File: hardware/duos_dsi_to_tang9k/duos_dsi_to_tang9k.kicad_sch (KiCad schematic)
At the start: 6 parts, among them J1 Duo_S_DSI_IN, J2 Tang_Nano_9K

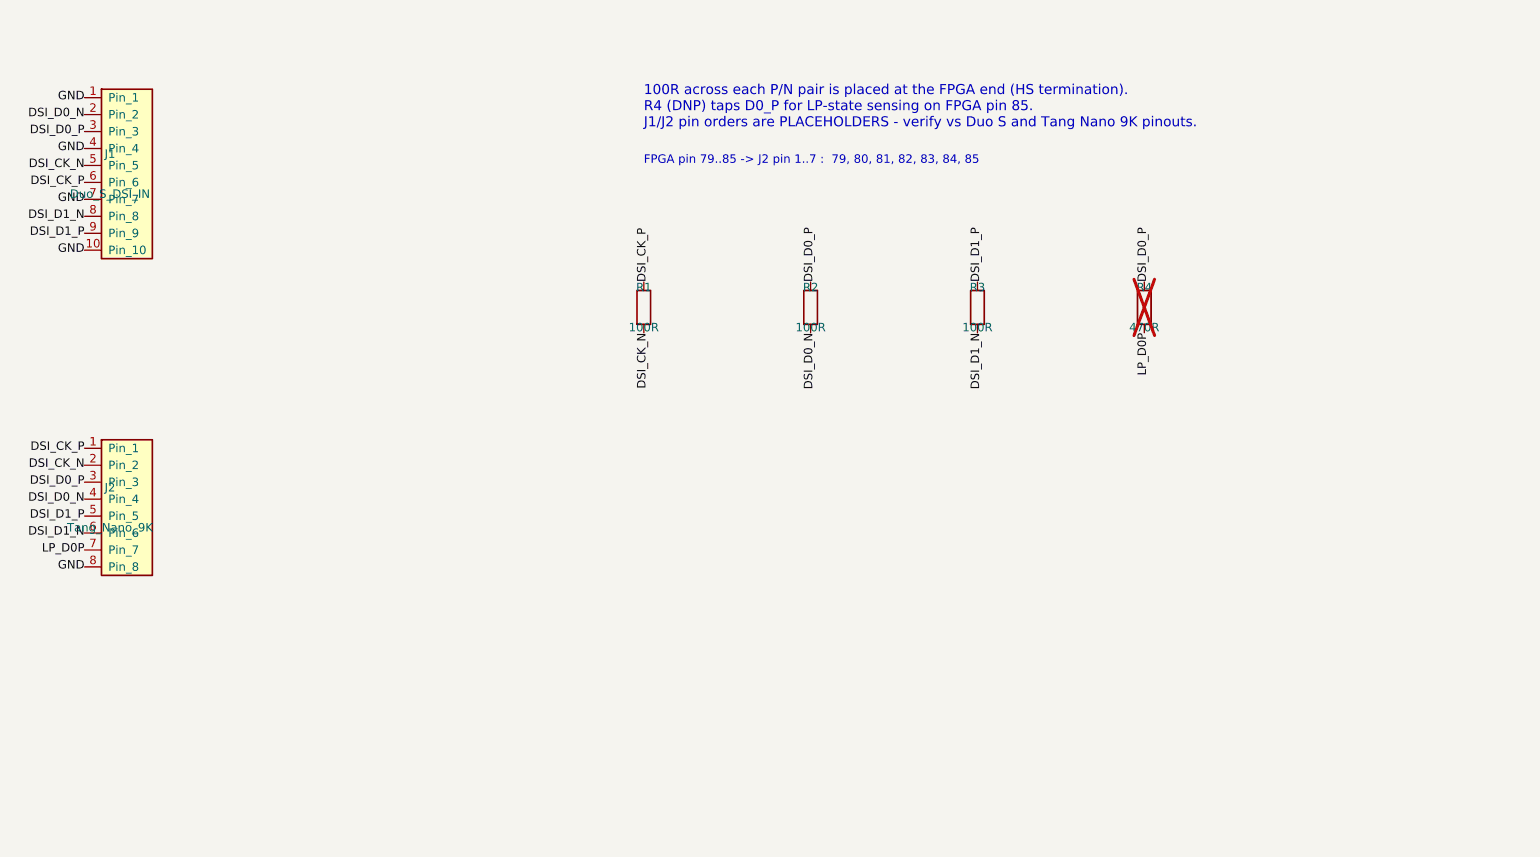
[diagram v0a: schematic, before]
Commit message: Use real Duo S CON26A MIPI_TX pinout in DSI adapter project
Co-Authored-By: Claude Sonnet 5.5 <noreply@anthropic.com>
Claude-Session: https://claude.ai/code/session_01Kmp7iiQhgLgwfNawdP6KaV
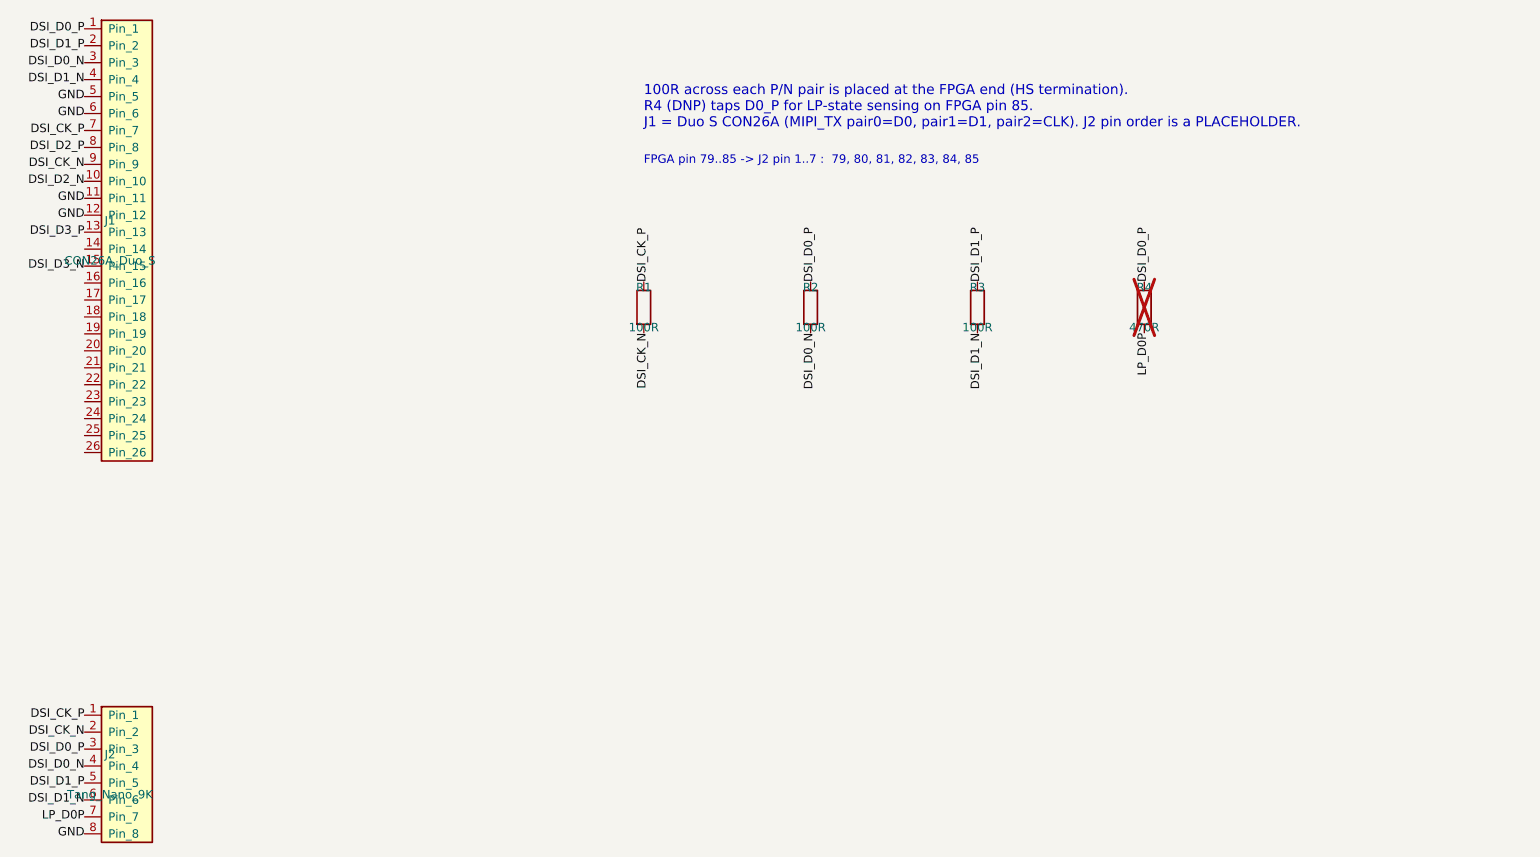
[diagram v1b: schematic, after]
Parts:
- removed J1: Duo_S_DSI_IN, Connector_PinHeader_2.54mm:PinHeader_1x10_P2.54mm_Vertical, symbol Connector_Generic:Conn_01x10
- added J1: CON26A_Duo_S, Connector_PinHeader_2.54mm:PinHeader_2x13_P2.54mm_Vertical, symbol Connector_Generic:Conn_01x26
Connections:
- net DSI_CK_N: now also J1.9 (Pin_9)
- net DSI_CK_P: now also J1.7 (Pin_7)
- net DSI_D0_N: now also J1.3 (Pin_3)
- net DSI_D0_P: now also J1.1 (Pin_1)
- net DSI_D1_N: now also J1.4 (Pin_4)
- net DSI_D1_P: now also J1.2 (Pin_2)
- net GND: now also J1.11 (Pin_11), J1.12 (Pin_12), J1.5 (Pin_5), J1.6 (Pin_6)
- new net DSI_D2_N: J1.10 (Pin_10)
- new net DSI_D2_P: J1.8 (Pin_8)
- new net DSI_D3_N: J1.15 (Pin_15)
- new net DSI_D3_P: J1.13 (Pin_13)
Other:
- note added: "100R across each P/N pair is placed at the FPGA end (HS termination). R4 (DNP) taps D0_P for LP-state sensing on FPGA pin 85. J1 = Duo S CON26A (MIPI_TX pair0=D0, pair1=D1, pair2=CLK). J2 pin order is a PLACEHOLDER."
- note removed: "100R across each P/N pair is placed at the FPGA end (HS termination). R4 (DNP) taps D0_P for LP-state sensing on FPGA pin 85. J1/J2 pin orders are PLACEHOLDERS - verify vs Duo S and Tang Nano 9K pinouts."
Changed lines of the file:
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@@
 (kicad_sch (version 20230121) (generator "gen_project.py") (paper "A4")
-(symbol (lib_id "Connector_Generic:Conn_01x10") (at 60 80 0) (unit 1) (in_bom yes) (on_board yes) (dnp no)
-(property "Reference" "J1" (at 60 77 0) (effects (font (size 1.27 1.27))))
-(property "Value" "Duo_S_DSI_IN" (at 60 83 0) (effects (font (size 1.27 1.27))))
-(property "Footprint" "Connector_PinHeader_2.54mm:PinHeader_1x10_P2.54mm_Vertical" (at 60 80 0) (effects (font (size 1.27 1.27)) hide))
-(pin "1")(pin "2")(pin "3")(pin "4")(pin "5")(pin "6")(pin "7")(pin "8")(pin "9")(pin "10")
-(instances (project "duos_dsi_to_tang9k" (path "/370e3fb2-c56f-42e8-af79-f2a3169dccd3" (reference "J1") (unit 1)))))
-(label "GND" (at 56.19 68.57 180) (effects (font (size 1.27 1.27)) (justify right)))
-(label "DSI_D0_N" (at 56.19 71.11 180) (effects (font (size 1.27 1.27)) (justify right)))
-(label "DSI_D0_P" (at 56.19 73.65 180) (effects (font (size 1.27 1.27)) (justify right)))
-(label "GND" (at 56.19 76.19 180) (effects (font (size 1.27 1.27)) (justify right)))
-(label "DSI_CK_N" (at 56.19 78.73 180) (effects (font (size 1.27 1.27)) (justify right)))
-(label "DSI_CK_P" (at 56.19 81.27 180) (effects (font (size 1.27 1.27)) (justify right)))
-(label "GND" (at 56.19 83.81 180) (effects (font (size 1.27 1.27)) (justify right)))
-(label "DSI_D1_N" (at 56.19 86.35 180) (effects (font (size 1.27 1.27)) (justify right)))
-(label "DSI_D1_P" (at 56.19 88.89 180) (effects (font (size 1.27 1.27)) (justify right)))
-(label "GND" (at 56.19 91.43 180) (effects (font (size 1.27 1.27)) (justify right)))
-(symbol (lib_id "Connector_Generic:Conn_01x08") (at 60 130 0) (unit 1) (in_bom yes) (on_board yes) (dnp no)
-(property "Reference" "J2" (at 60 127 0) (effects (font (size 1.27 1.27))))
-(property "Value" "Tang_Nano_9K" (at 60 133 0) (effects (font (size 1.27 1.27))))
-(property "Footprint" "Connector_PinHeader_2.54mm:PinHeader_1x08_P2.54mm_Vertical" (at 60 130 0) (effects (font (size 1.27 1.27)) hide))
+(symbol (lib_id "Connector_Generic:Conn_01x26") (at 60 90 0) (unit 1) (in_bom yes) (on_board yes) (dnp no)
+(property "Reference" "J1" (at 60 87 0) (effects (font (size 1.27 1.27))))
+(property "Value" "CON26A_Duo_S" (at 60 93 0) (effects (font (size 1.27 1.27))))
+(property "Footprint" "Connector_PinHeader_2.54mm:PinHeader_2x13_P2.54mm_Vertical" (at 60 90 0) (effects (font (size 1.27 1.27)) hide))
+(pin "1")(pin "2")(pin "3")(pin "4")(pin "5")(pin "6")(pin "7")(pin "8")(pin "9")(pin "10")(pin "11")(pin "12")(pin "13")(pin "14")(pin "15")(pin "16")(pin "17")(pin "18")(pin "19")(pin "20")(pin "21")(pin "22")(pin "23")(pin "24")(pin "25")(pin "26")
+(instances (project "duos_dsi_to_tang9k" (path "/7ba3984c-b53a-427d-af08-25dba6ae9ceb" (reference "J1") (unit 1)))))
+(label "DSI_D0_P" (at 56.19 58.25 180) (effects (font (size 1.27 1.27)) (justify right)))
+(label "DSI_D1_P" (at 56.19 60.79 180) (effects (font (size 1.27 1.27)) (justify right)))
+(label "DSI_D0_N" (at 56.19 63.33 180) (effects (font (size 1.27 1.27)) (justify right)))
+(label "DSI_D1_N" (at 56.19 65.87 180) (effects (font (size 1.27 1.27)) (justify right)))
+(label "GND" (at 56.19 68.41 180) (effects (font (size 1.27 1.27)) (justify right)))
+(label "GND" (at 56.19 70.95 180) (effects (font (size 1.27 1.27)) (justify right)))
+(label "DSI_CK_P" (at 56.19 73.49 180) (effects (font (size 1.27 1.27)) (justify right)))
+(label "DSI_D2_P" (at 56.19 76.03 180) (effects (font (size 1.27 1.27)) (justify right)))
+(label "DSI_CK_N" (at 56.19 78.57 180) (effects (font (size 1.27 1.27)) (justify right)))
+(label "DSI_D2_N" (at 56.19 81.11 180) (effects (font (size 1.27 1.27)) (justify right)))
+(label "GND" (at 56.19 83.65 180) (effects (font (size 1.27 1.27)) (justify right)))
+(label "GND" (at 56.19 86.19 180) (effects (font (size 1.27 1.27)) (justify right)))
+(label "DSI_D3_P" (at 56.19 88.73 180) (effects (font (size 1.27 1.27)) (justify right)))
+(label "DSI_D3_N" (at 56.19 93.81 180) (effects (font (size 1.27 1.27)) (justify right)))
+(symbol (lib_id "Connector_Generic:Conn_01x08") (at 60 170 0) (unit 1) (in_bom yes) (on_board yes) (dnp no)
+(property "Reference" "J2" (at 60 167 0) (effects (font (size 1.27 1.27))))
+(property "Value" "Tang_Nano_9K" (at 60 173 0) (effects (font (size 1.27 1.27))))
+(property "Footprint" "Connector_PinHeader_2.54mm:PinHeader_1x08_P2.54mm_Vertical" (at 60 170 0) (effects (font (size 1.27 1.27)) hide))
 (pin "1")(pin "2")(pin "3")(pin "4")(pin "5")(pin "6")(pin "7")(pin "8")
-(instances (project "duos_dsi_to_tang9k" (path "/370e3fb2-c56f-42e8-af79-f2a3169dccd3" (reference "J2") (unit 1)))))
-(label "DSI_CK_P" (at 56.19 121.11 180) (effects (font (size 1.27 1.27)) (justify right)))
-(label "DSI_CK_N" (at 56.19 123.65 180) (effects (font (size 1.27 1.27)) (justify right)))
-(label "DSI_D0_P" (at 56.19 126.19 180) (effects (font (size 1.27 1.27)) (justify right)))
-(label "DSI_D0_N" (at 56.19 128.73 180) (effects (font (size 1.27 1.27)) (justify right)))
-(label "DSI_D1_P" (at 56.19 131.27 180) (effects (font (size 1.27 1.27)) (justify right)))
-(label "DSI_D1_N" (at 56.19 133.81 180) (effects (font (size 1.27 1.27)) (justify right)))
-(label "LP_D0P" (at 56.19 136.35 180) (effects (font (size 1.27 1.27)) (justify right)))
-(label "GND" (at 56.19 138.89 180) (effects (font (size 1.27 1.27)) (justify right)))
+(instances (project "duos_dsi_to_tang9k" (path "/7ba3984c-b53a-427d-af08-25dba6ae9ceb" (reference "J2") (unit 1)))))
+(label "DSI_CK_P" (at 56.19 161.11 180) (effects (font (size 1.27 1.27)) (justify right)))
+(label "DSI_CK_N" (at 56.19 163.65 180) (effects (font (size 1.27 1.27)) (justify right)))
+(label "DSI_D0_P" (at 56.19 166.19 180) (effects (font (size 1.27 1.27)) (justify right)))
+(label "DSI_D0_N" (at 56.19 168.73 180) (effects (font (size 1.27 1.27)) (justify right)))
+(label "DSI_D1_P" (at 56.19 171.27 180) (effects (font (size 1.27 1.27)) (justify right)))
+(label "DSI_D1_N" (at 56.19 173.81 180) (effects (font (size 1.27 1.27)) (justify right)))
+(label "LP_D0P" (at 56.19 176.35 180) (effects (font (size 1.27 1.27)) (justify right)))
+(label "GND" (at 56.19 178.89 180) (effects (font (size 1.27 1.27)) (justify right)))
 (symbol (lib_id "Device:R") (at 140 100 0) (unit 1) (in_bom yes) (on_board yes) (dnp no)
 (property "Reference" "R1" (at 140 97 0) (effects (font (size 1.27 1.27))))
@@
 (property "Footprint" "Resistor_SMD:R_0402_1005Metric" (at 140 100 0) (effects (font (size 1.27 1.27)) hide))
 (pin "1")(pin "2")
-(instances (project "duos_dsi_to_tang9k" (path "/370e3fb2-c56f-42e8-af79-f2a3169dccd3" (reference "R1") (unit 1)))))
+(instances (project "duos_dsi_to_tang9k" (path "/7ba3984c-b53a-427d-af08-25dba6ae9ceb" (reference "R1") (unit 1)))))
 (label "DSI_CK_P" (at 140.00 96.19 90) (effects (font (size 1.27 1.27))))
 (label "DSI_CK_N" (at 140.00 103.81 270) (effects (font (size 1.27 1.27))))
@@
 (property "Footprint" "Resistor_SMD:R_0402_1005Metric" (at 165 100 0) (effects (font (size 1.27 1.27)) hide))
 (pin "1")(pin "2")
-(instances (project "duos_dsi_to_tang9k" (path "/370e3fb2-c56f-42e8-af79-f2a3169dccd3" (reference "R2") (unit 1)))))
+(instances (project "duos_dsi_to_tang9k" (path "/7ba3984c-b53a-427d-af08-25dba6ae9ceb" (reference "R2") (unit 1)))))
 (label "DSI_D0_P" (at 165.00 96.19 90) (effects (font (size 1.27 1.27))))
 (label "DSI_D0_N" (at 165.00 103.81 270) (effects (font (size 1.27 1.27))))
@@
 (property "Footprint" "Resistor_SMD:R_0402_1005Metric" (at 190 100 0) (effects (font (size 1.27 1.27)) hide))
 (pin "1")(pin "2")
-(instances (project "duos_dsi_to_tang9k" (path "/370e3fb2-c56f-42e8-af79-f2a3169dccd3" (reference "R3") (unit 1)))))
+(instances (project "duos_dsi_to_tang9k" (path "/7ba3984c-b53a-427d-af08-25dba6ae9ceb" (reference "R3") (unit 1)))))
 (label "DSI_D1_P" (at 190.00 96.19 90) (effects (font (size 1.27 1.27))))
 (label "DSI_D1_N" (at 190.00 103.81 270) (effects (font (size 1.27 1.27))))
@@
 (property "Footprint" "Resistor_SMD:R_0402_1005Metric" (at 215 100 0) (effects (font (size 1.27 1.27)) hide))
 (pin "1")(pin "2")
-(instances (project "duos_dsi_to_tang9k" (path "/370e3fb2-c56f-42e8-af79-f2a3169dccd3" (reference "R4") (unit 1)))))
+(instances (project "duos_dsi_to_tang9k" (path "/7ba3984c-b53a-427d-af08-25dba6ae9ceb" (reference "R4") (unit 1)))))
 (label "DSI_D0_P" (at 215.00 96.19 90) (effects (font (size 1.27 1.27))))
 (label "LP_D0P" (at 215.00 103.81 270) (effects (font (size 1.27 1.27))))
-(text "100R across each P/N pair is placed at the FPGA end (HS termination).\nR4 (DNP) taps D0_P for LP-state sensing on FPGA pin 85.\nJ1/J2 pin orders are PLACEHOLDERS - verify vs Duo S and Tang Nano 9K pinouts." (at 140 70 0) (effects (font (size 1.5 1.5)) (justify left)))
+(text "100R across each P/N pair is placed at the FPGA end (HS termination).\nR4 (DNP) taps D0_P for LP-state sensing on FPGA pin 85.\nJ1 = Duo S CON26A (MIPI_TX pair0=D0, pair1=D1, pair2=CLK). J2 pin order is a PLACEHOLDER." (at 140 70 0) (effects (font (size 1.5 1.5)) (justify left)))
 (text "FPGA pin 79..85 -> J2 pin 1..7 :  79, 80, 81, 82, 83, 84, 85" (at 140 78 0) (effects (font (size 1.27 1.27)) (justify left)))
 (sheet_instances (path "/" (page "1"))))
